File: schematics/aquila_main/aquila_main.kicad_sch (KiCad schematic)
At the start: 109 parts

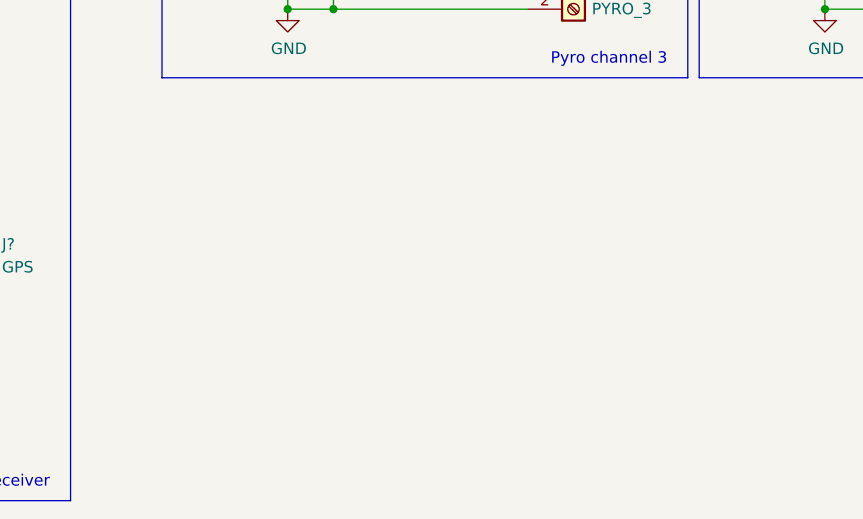
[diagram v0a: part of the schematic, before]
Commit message: added mounting holes
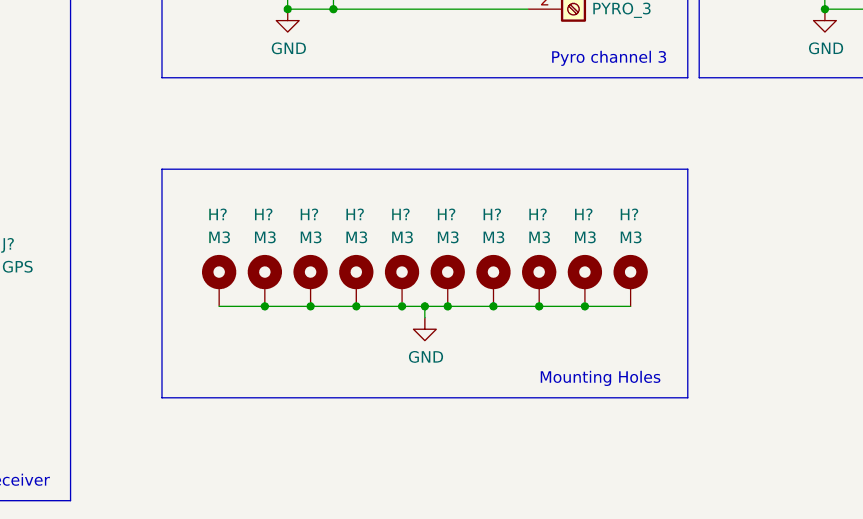
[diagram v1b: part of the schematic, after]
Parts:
- added H? (x10): M3, MountingHole:MountingHole_3.2mm_M3_DIN965_Pad, symbol Mechanical:MountingHole_Pad
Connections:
- net GND: now also H?.1, H?.1, H?.1, H?.1, H?.1, H?.1, H?.1, H?.1, H?.1, H?.1
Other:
- note added: "Mounting Holes"

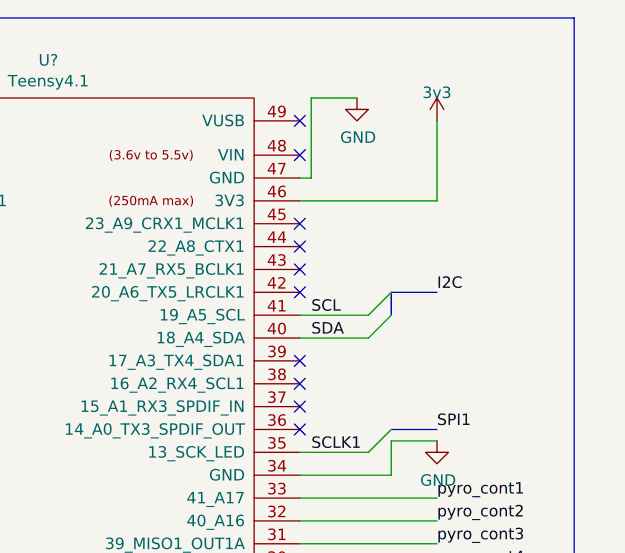
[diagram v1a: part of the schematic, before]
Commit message: added I2C pullups
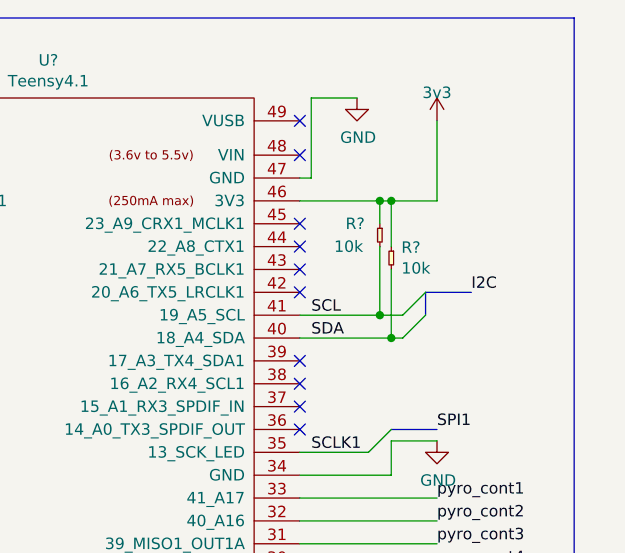
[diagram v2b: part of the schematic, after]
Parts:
- added R? (x2): 10k, symbol aquila:R-cusf-kicad
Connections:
- net +3V3: now also R?.1, R?.1
- net SCL: now also R?.2
- net SDA: now also R?.2
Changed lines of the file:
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@@
   (junction (at 120.65 257.81) (diameter 0) (color 0 0 0 0)
   )
+  (junction (at 312.42 48.26) (diameter 0) (color 0 0 0 0)
+  )
   (junction (at 251.46 190.5) (diameter 0) (color 0 0 0 0)
   )
@@
   (junction (at 237.49 247.65) (diameter 0) (color 0 0 0 0)
   )
+  (junction (at 313.69 63.5) (diameter 0) (color 0 0 0 0)
+  )
   (junction (at 60.96 40.64) (diameter 0) (color 0 0 0 0)
   )
@@
   (junction (at 95.25 113.03) (diameter 0) (color 0 0 0 0)
   )
+  (junction (at 313.69 48.26) (diameter 0) (color 0 0 0 0)
+  )
   (junction (at 262.89 247.65) (diameter 0) (color 0 0 0 0)
   )
@@
   (junction (at 232.41 247.65) (diameter 0) (color 0 0 0 0)
   )
+  (junction (at 312.42 60.96) (diameter 0) (color 0 0 0 0)
+  )
   (junction (at 48.26 219.71) (diameter 0) (color 0 0 0 0)
   )
@@
     (stroke (width 0) (type default) (color 0 0 0 0))
   )
-  (bus_entry (at 311.15 60.96) (size 2.54 -2.54)
+  (bus_entry (at 314.96 60.96) (size 2.54 -2.54)
     (stroke (width 0) (type default) (color 0 0 0 0))
   )
@@
     (stroke (width 0) (type default) (color 0 0 0 0))
   )
-  (bus_entry (at 311.15 63.5) (size 2.54 -2.54)
+  (bus_entry (at 314.96 63.5) (size 2.54 -2.54)
     (stroke (width 0) (type default) (color 0 0 0 0))
   )
@@
     (stroke (width 0) (type default) (color 0 0 0 0))
   )
+  (wire (pts (xy 312.42 53.34) (xy 312.42 60.96))
+    (stroke (width 0) (type default) (color 0 0 0 0))
+  )
   (wire (pts (xy 102.87 241.3) (xy 102.87 243.84))
     (stroke (width 0) (type default) (color 0 0 0 0))
@@
     (stroke (width 0) (type default) (color 0 0 0 0))
   )
+  (wire (pts (xy 313.69 48.26) (xy 318.77 48.26))
+    (stroke (width 0) (type default) (color 0 0 0 0))
+  )
   (wire (pts (xy 231.14 53.34) (xy 247.65 53.34))
     (stroke (width 0) (type default) (color 0 0 0 0))
@@
     (stroke (width 0) (type default) (color 0 0 0 0))
   )
+  (wire (pts (xy 313.69 63.5) (xy 314.96 63.5))
+    (stroke (width 0) (type default) (color 0 0 0 0))
+  )
   (wire (pts (xy 303.53 99.06) (xy 318.77 99.06))
     (stroke (width 0) (type default) (color 0 0 0 0))
@@
     (stroke (width 0) (type default) (color 0 0 0 0))
   )
-  (wire (pts (xy 303.53 60.96) (xy 311.15 60.96))
+  (wire (pts (xy 303.53 60.96) (xy 312.42 60.96))
     (stroke (width 0) (type default) (color 0 0 0 0))
   )
@@
     (stroke (width 0) (type default) (color 0 0 0 0))
   )
+  (wire (pts (xy 312.42 48.26) (xy 313.69 48.26))
+    (stroke (width 0) (type default) (color 0 0 0 0))
+  )
   (bus (pts (xy 58.42 184.15) (xy 58.42 186.69))
     (stroke (width 0) (type default) (color 0 0 0 0))
@@
     (stroke (width 0) (type default) (color 0 0 0 0))
   )
-  (bus (pts (xy 313.69 60.96) (xy 313.69 58.42))
+  (bus (pts (xy 317.5 60.96) (xy 317.5 58.42))
     (stroke (width 0) (type default) (color 0 0 0 0))
   )
@@
     (stroke (width 0) (type default) (color 0 0 0 0))
   )
+  (wire (pts (xy 312.42 60.96) (xy 314.96 60.96))
+    (stroke (width 0) (type default) (color 0 0 0 0))
+  )
   (wire (pts (xy 187.96 36.83) (xy 187.96 39.37))
     (stroke (width 0) (type default) (color 0 0 0 0))
@@
     (stroke (width 0) (type default) (color 0 0 0 0))
   )
+  (wire (pts (xy 303.53 48.26) (xy 312.42 48.26))
+    (stroke (width 0) (type default) (color 0 0 0 0))
+  )
   (wire (pts (xy 316.23 154.94) (xy 316.23 160.02))
     (stroke (width 0) (type default) (color 0 0 0 0))
@@
     (stroke (width 0) (type default) (color 0 0 0 0))
   )
+  (wire (pts (xy 312.42 48.26) (xy 312.42 50.8))
+    (stroke (width 0) (type default) (color 0 0 0 0))
+  )
   (wire (pts (xy 294.64 190.5) (xy 285.75 190.5))
     (stroke (width 0) (type default) (color 0 0 0 0))
@@
     (stroke (width 0) (type default) (color 0 0 0 0))
   )
-  (wire (pts (xy 303.53 63.5) (xy 311.15 63.5))
+  (wire (pts (xy 303.53 63.5) (xy 313.69 63.5))
     (stroke (width 0) (type default) (color 0 0 0 0))
   )
@@
     (stroke (width 0) (type default) (color 0 0 0 0))
   )
-  (wire (pts (xy 303.53 48.26) (xy 318.77 48.26))
-    (stroke (width 0) (type default) (color 0 0 0 0))
-  )
   (wire (pts (xy 151.13 175.26) (xy 153.67 175.26))
     (stroke (width 0) (type default) (color 0 0 0 0))
@@
     (stroke (width 0) (type default) (color 0 0 0 0))
   )
+  (wire (pts (xy 313.69 48.26) (xy 313.69 53.34))
+    (stroke (width 0) (type default) (color 0 0 0 0))
+  )
   (polyline (pts (xy 205.74 142.24) (xy 175.26 142.24))
     (stroke (width 0) (type default) (color 0 0 0 0))
@@
     (stroke (width 0) (type default) (color 0 0 0 0))
   )
-  (bus (pts (xy 313.69 58.42) (xy 318.77 58.42))
+  (bus (pts (xy 317.5 58.42) (xy 322.58 58.42))
     (stroke (width 0) (type default) (color 0 0 0 0))
   )
@@
     (stroke (width 0) (type default) (color 0 0 0 0))
   )
+  (wire (pts (xy 313.69 55.88) (xy 313.69 63.5))
+    (stroke (width 0) (type default) (color 0 0 0 0))
+  )
   (wire (pts (xy 231.14 58.42) (xy 247.65 58.42))
     (stroke (width 0) (type default) (color 0 0 0 0))
@@
     (effects (font (size 1.27 1.27)) (justify left bottom))
   )
-  (label "I2C" (at 318.77 58.42 0)
+  (label "I2C" (at 322.58 58.42 0)
     (effects (font (size 1.27 1.27)) (justify left bottom))
   )
@@
     (pin "2")
   )
+  (symbol (lib_id "aquila:R-cusf-kicad") (at 312.42 50.8 270) (unit 1)
+    (in_bom yes) (on_board yes)
+    (property "Reference" "R?" (id 0) (at 308.61 50.8 90)
+      (effects (font (size 1.27 1.27)) (justify left))
+    )
+    (property "Value" "10k" (id 1) (at 307.34 53.34 90)
+      (effects (font (size 1.27 1.27)) (justify left))
+    )
+    (property "Footprint" "" (id 2) (at 312.42 50.8 0)
+      (effects (font (size 1.27 1.27)) hide)
+    )
+    (property "Datasheet" "" (id 3) (at 312.42 50.8 0)
+      (effects (font (size 1.27 1.27)) hide)
+    )
+    (pin "1")
+    (pin "2")
+  )
   (symbol (lib_id "aquila:R-cusf-kicad") (at 132.08 243.84 270) (unit 1)
     (in_bom yes) (on_board yes)
@@
     (pin "8")
   )
+  (symbol (lib_id "aquila:R-cusf-kicad") (at 313.69 53.34 270) (unit 1)
+    (in_bom yes) (on_board yes)
+    (property "Reference" "R?" (id 0) (at 314.8076 53.4416 90)
+      (effects (font (size 1.27 1.27)) (justify left))
+    )
+    (property "Value" "10k" (id 1) (at 314.8076 55.753 90)
+      (effects (font (size 1.27 1.27)) (justify left))
+    )
+    (property "Footprint" "" (id 2) (at 313.69 53.34 0)
+      (effects (font (size 1.27 1.27)) hide)
+    )
+    (property "Datasheet" "" (id 3) (at 313.69 53.34 0)
+      (effects (font (size 1.27 1.27)) hide)
+    )
+    (pin "1")
+    (pin "2")
+  )
   (symbol (lib_name "IRF7509PbF_1") (lib_id "aquila:IRF7509PbF") (at 311.15 162.56 0) (unit 2)
     (in_bom yes) (on_board yes)
@@
       (reference "R?") (unit 1) (value "160") (footprint "")
     )
+    (path "/5d57a618-c8a9-4d13-a4d1-2e887e6e0a4c"
+      (reference "R?") (unit 1) (value "10k") (footprint "")
+    )
     (path "/5e64ef21-c0b3-4bc6-a310-da6f5fa019e8"
       (reference "R?") (unit 1) (value "DNP") (footprint "")
@@
       (reference "R?") (unit 1) (value "10k") (footprint "")
     )
+    (path "/c359ad78-6fe0-4f37-b251-002a3899e98c"
+      (reference "R?") (unit 1) (value "10k") (footprint "")
+    )

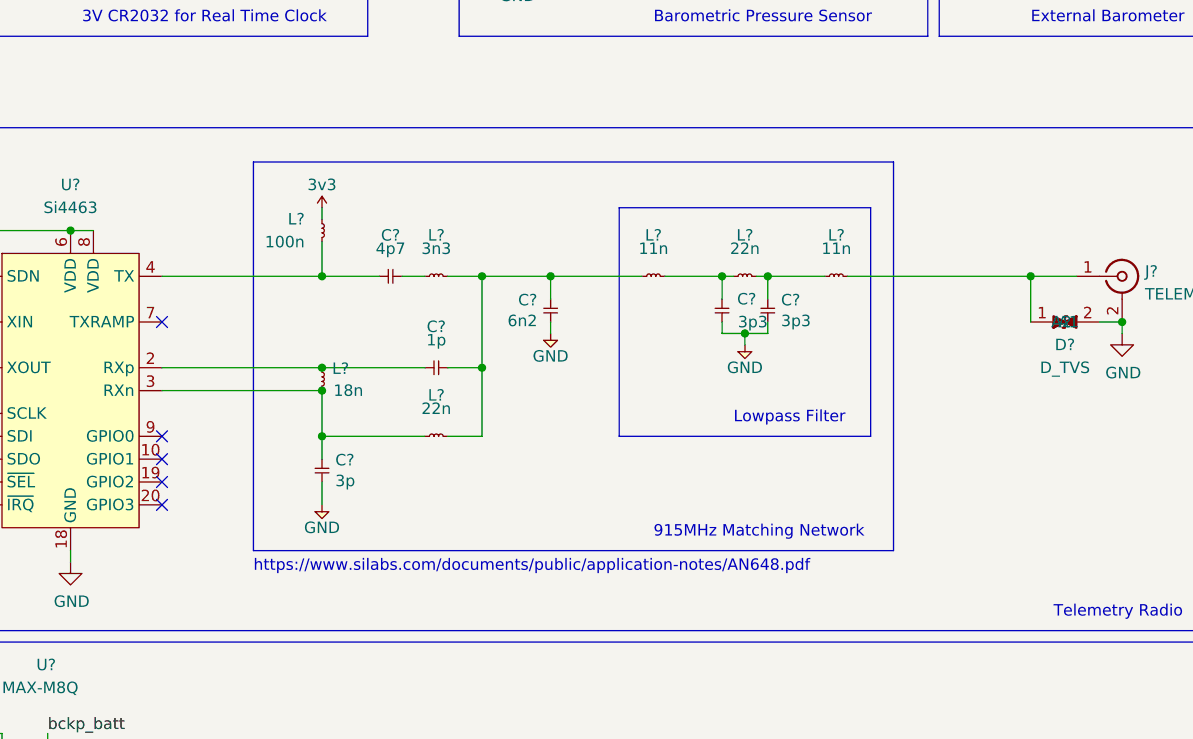
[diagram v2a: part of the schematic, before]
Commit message: added Pi pad to telem line
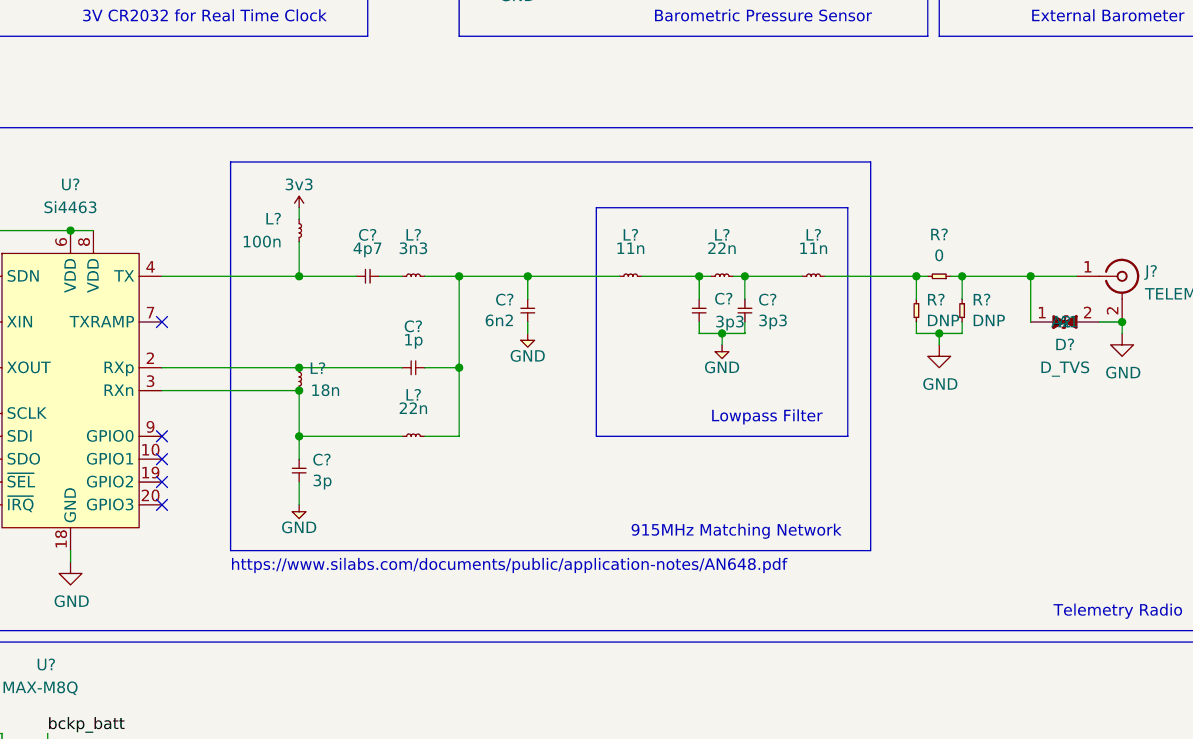
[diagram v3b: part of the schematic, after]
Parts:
- added R? (x2): DNP, symbol aquila:R-cusf-kicad
- added R?: 0, symbol aquila:R-cusf-kicad
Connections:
- net GND: now also R?.2, R?.2
- net at D?.1 (A1), J?.1 (In): now also R?.1, R?.1; no longer L?.2
- new net: L?.2, R?.1, R?.2
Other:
- moved on the sheet: C?, L?

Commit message: added footprint for BQ29200
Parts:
- U?: footprint (none) -> aquila:VSOP-8
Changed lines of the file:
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@@
       (effects (font (size 1.27 1.27)) (justify left))
     )
-    (property "Footprint" "" (id 2) (at 171.45 27.94 0)
+    (property "Footprint" "aquila:VSOP-8" (id 2) (at 171.45 27.94 0)
       (effects (font (size 1.27 1.27)) hide)
     )
@@
     )
     (path "/1ccc8a4d-7413-4368-95a1-68b18fd852c8"
-      (reference "U?") (unit 1) (value "BQ29200") (footprint "")
+      (reference "U?") (unit 1) (value "BQ29200") (footprint "aquila:VSOP-8")
     )
     (path "/29ade18c-a757-4c9f-86c8-3318f90f3aba"

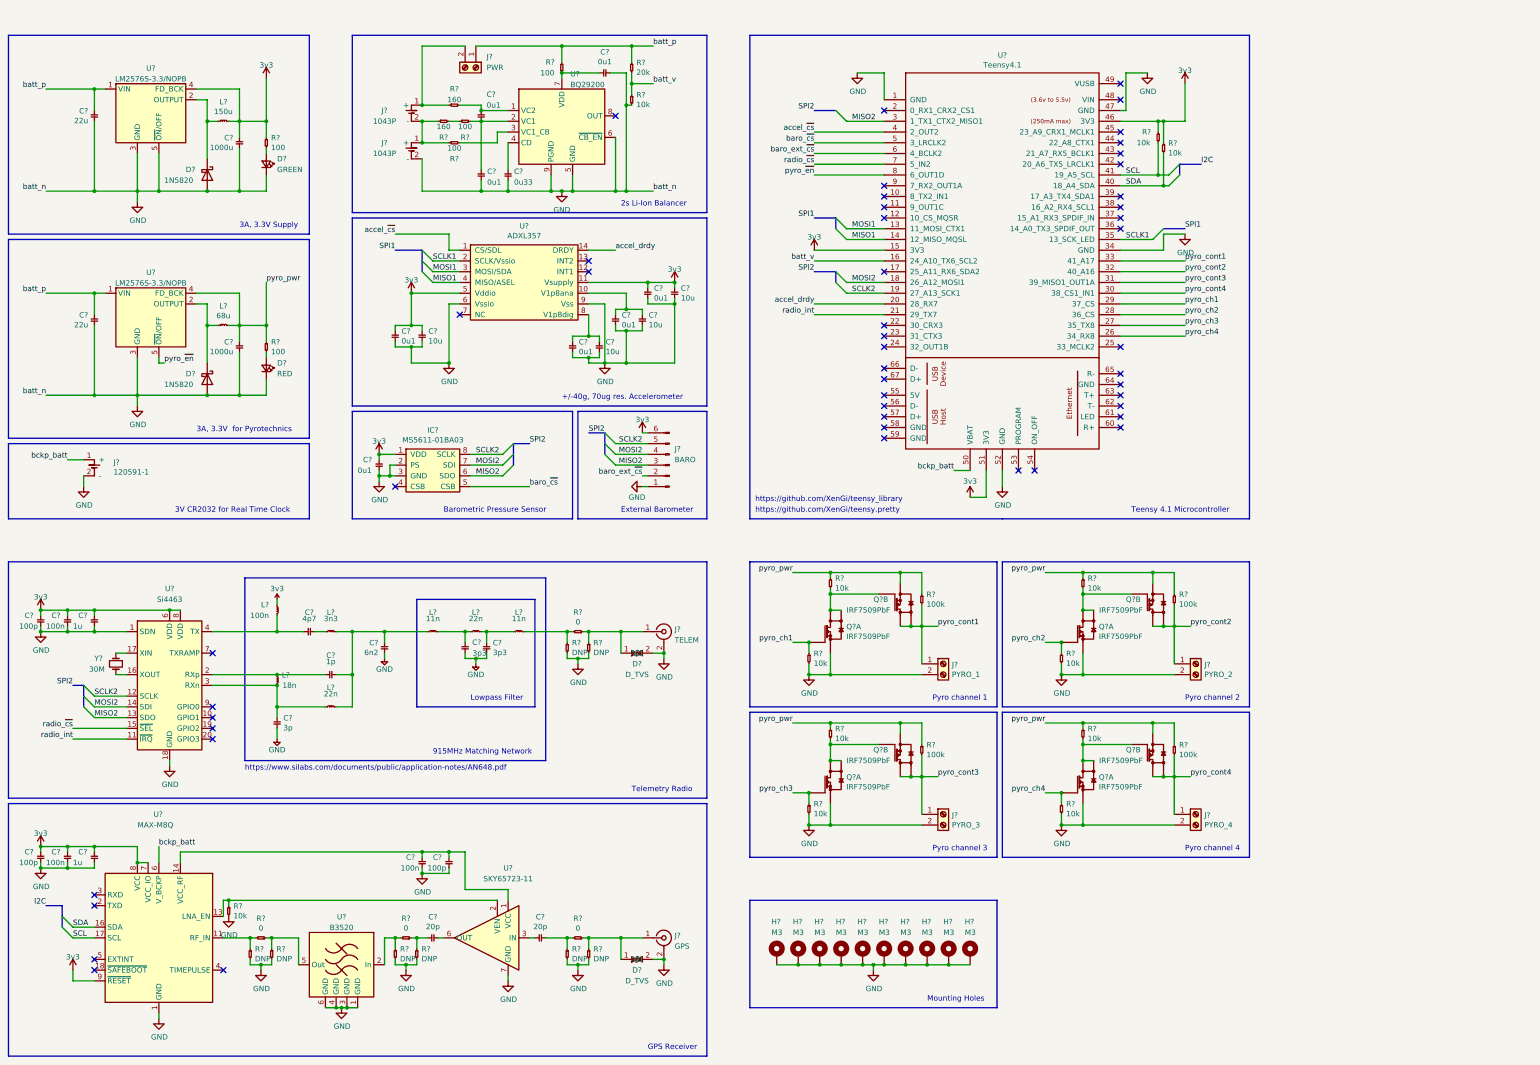
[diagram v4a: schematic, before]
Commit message: added RF shield
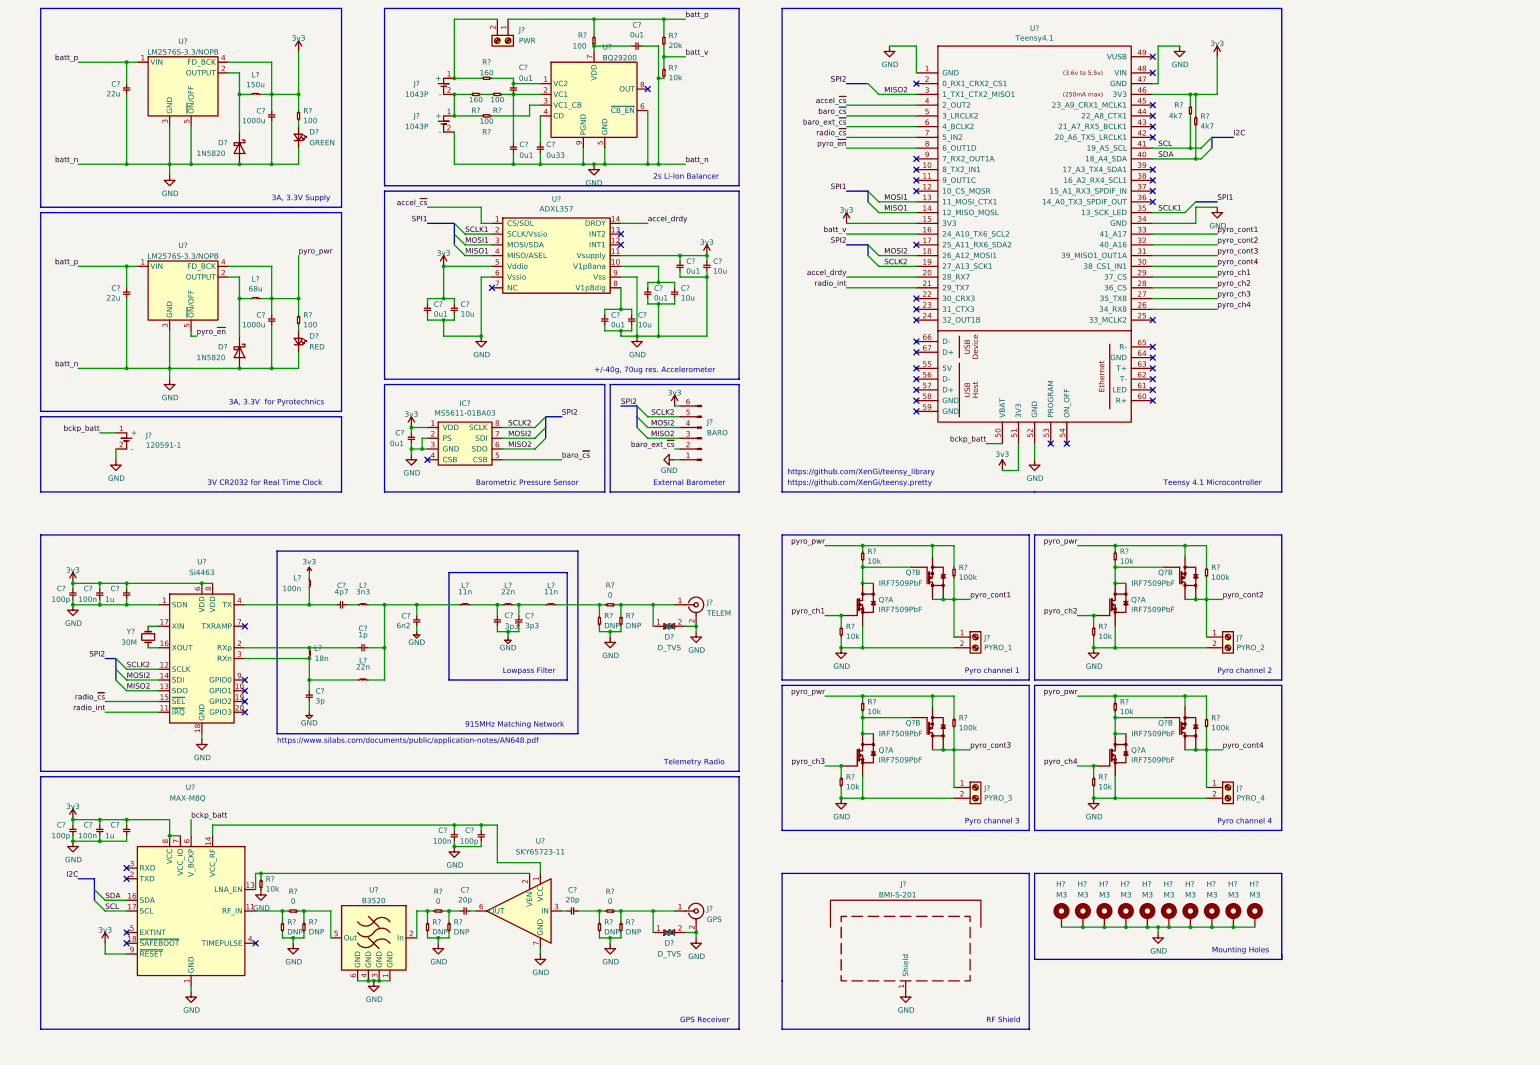
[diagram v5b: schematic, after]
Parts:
- added J?: BMI-S-201, aquila:BMI-S-201, symbol aquila:BMI-S-201
- R? (x2): value 10k -> 4k7
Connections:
- net GND: now also J?.1 (Shield)
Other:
- note added: "RF Shield"
- moved on the sheet: C?, D?, H?, IC?, J?, L?, Q?A, Q?B, R?, U?, Y?
